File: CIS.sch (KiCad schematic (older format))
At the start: 181 parts, among them J2 RJ45_Abracon_ARJP11A-MASA-B-A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, J3 SJ1-3533NG, J4 DEBUG TAG, K1 K_0073, K2 K_0072, P3 K_0023, Q1 Q_0002, Q2 Q_0002, Q3 Q_0002, SW1 SW_0003, SW2 SW_0003, SW3 SW_0003, SW4 SW_0003, SW5 SW_0003, U1 U_0076, U14 U_0101, U16 U_0049, U17 U_0049, U2 U_0131, U3 U_0103, U4 U_0134, U5 U_0081, U6 U_0097, U7 U_0132, U8 U_0133

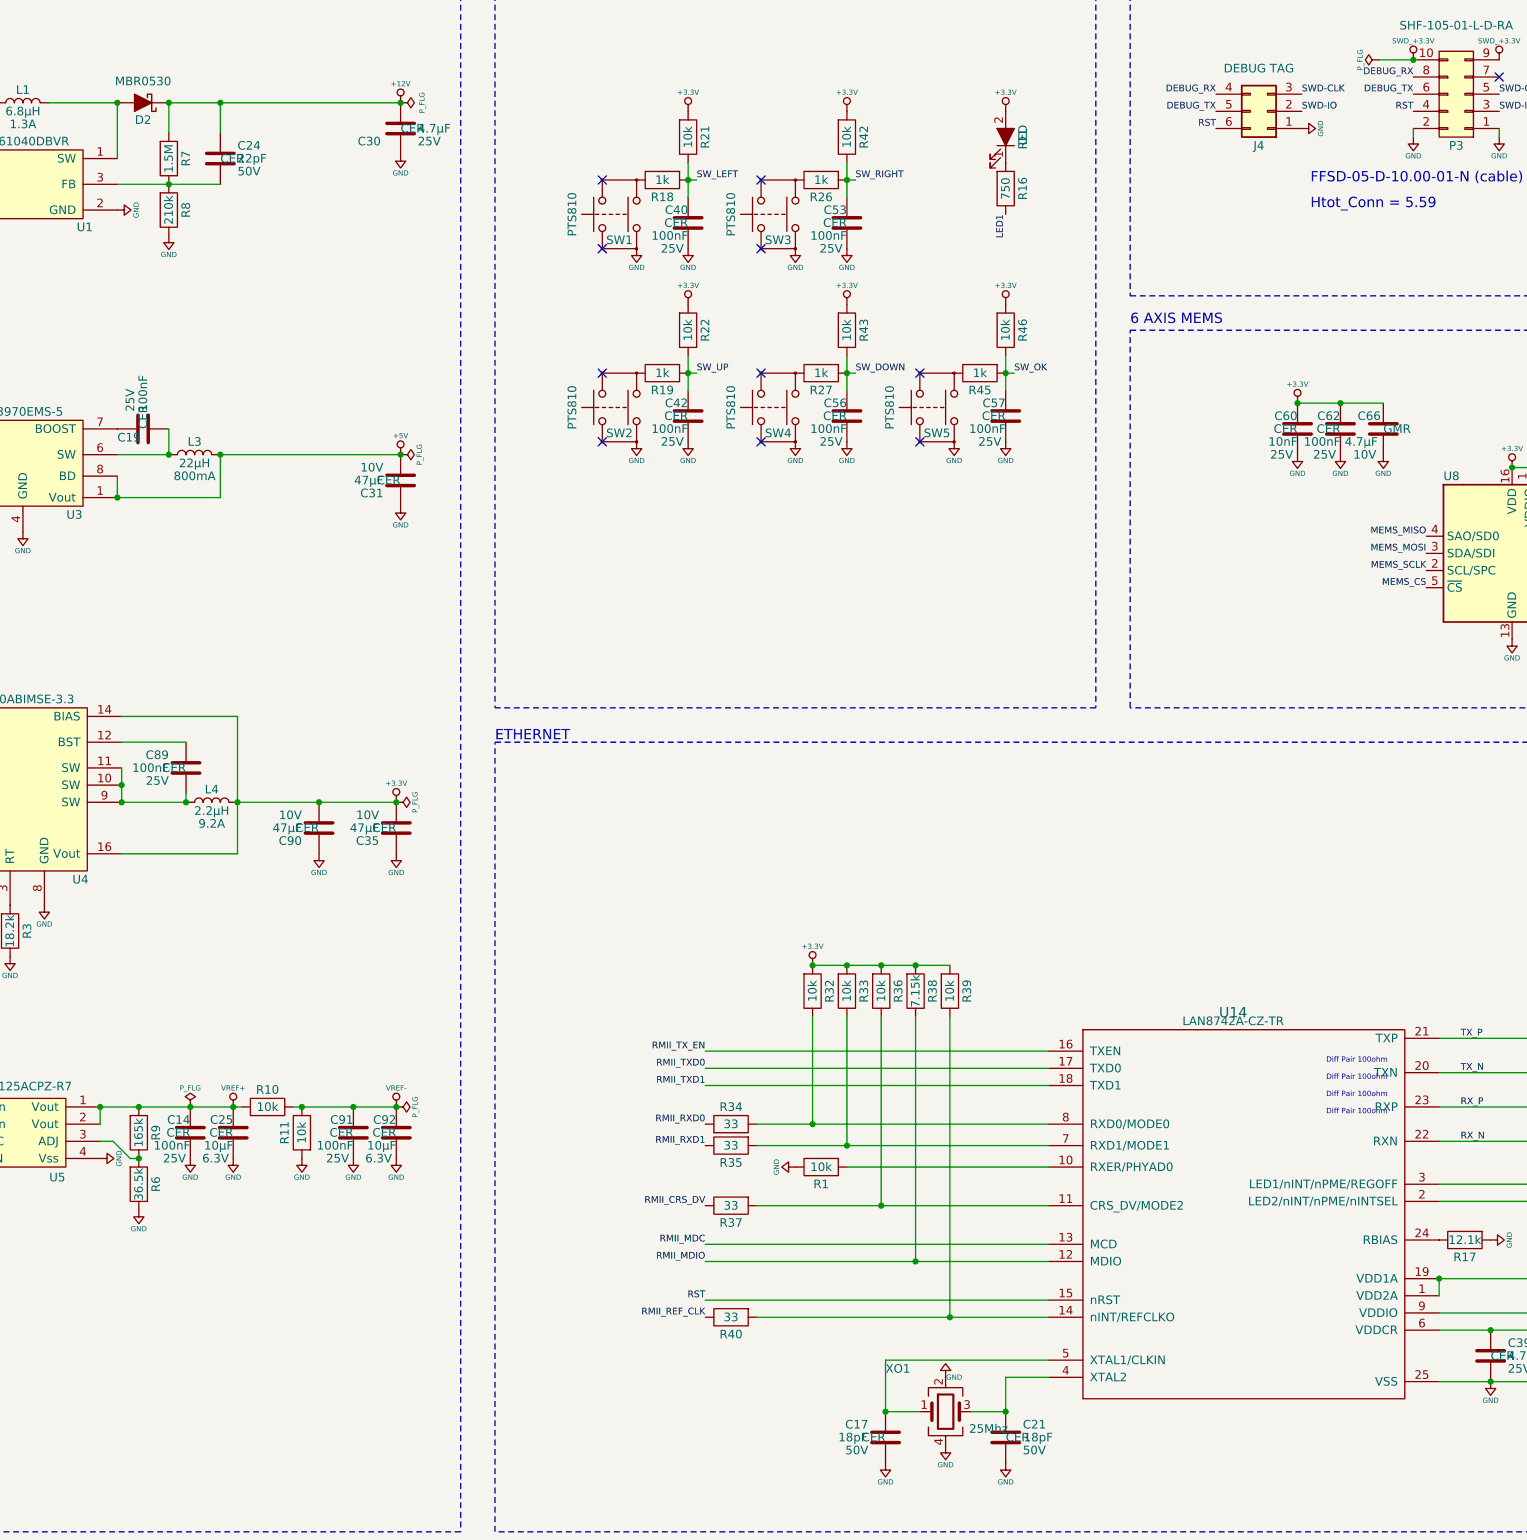
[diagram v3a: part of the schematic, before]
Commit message: Change some DC/DC resistors
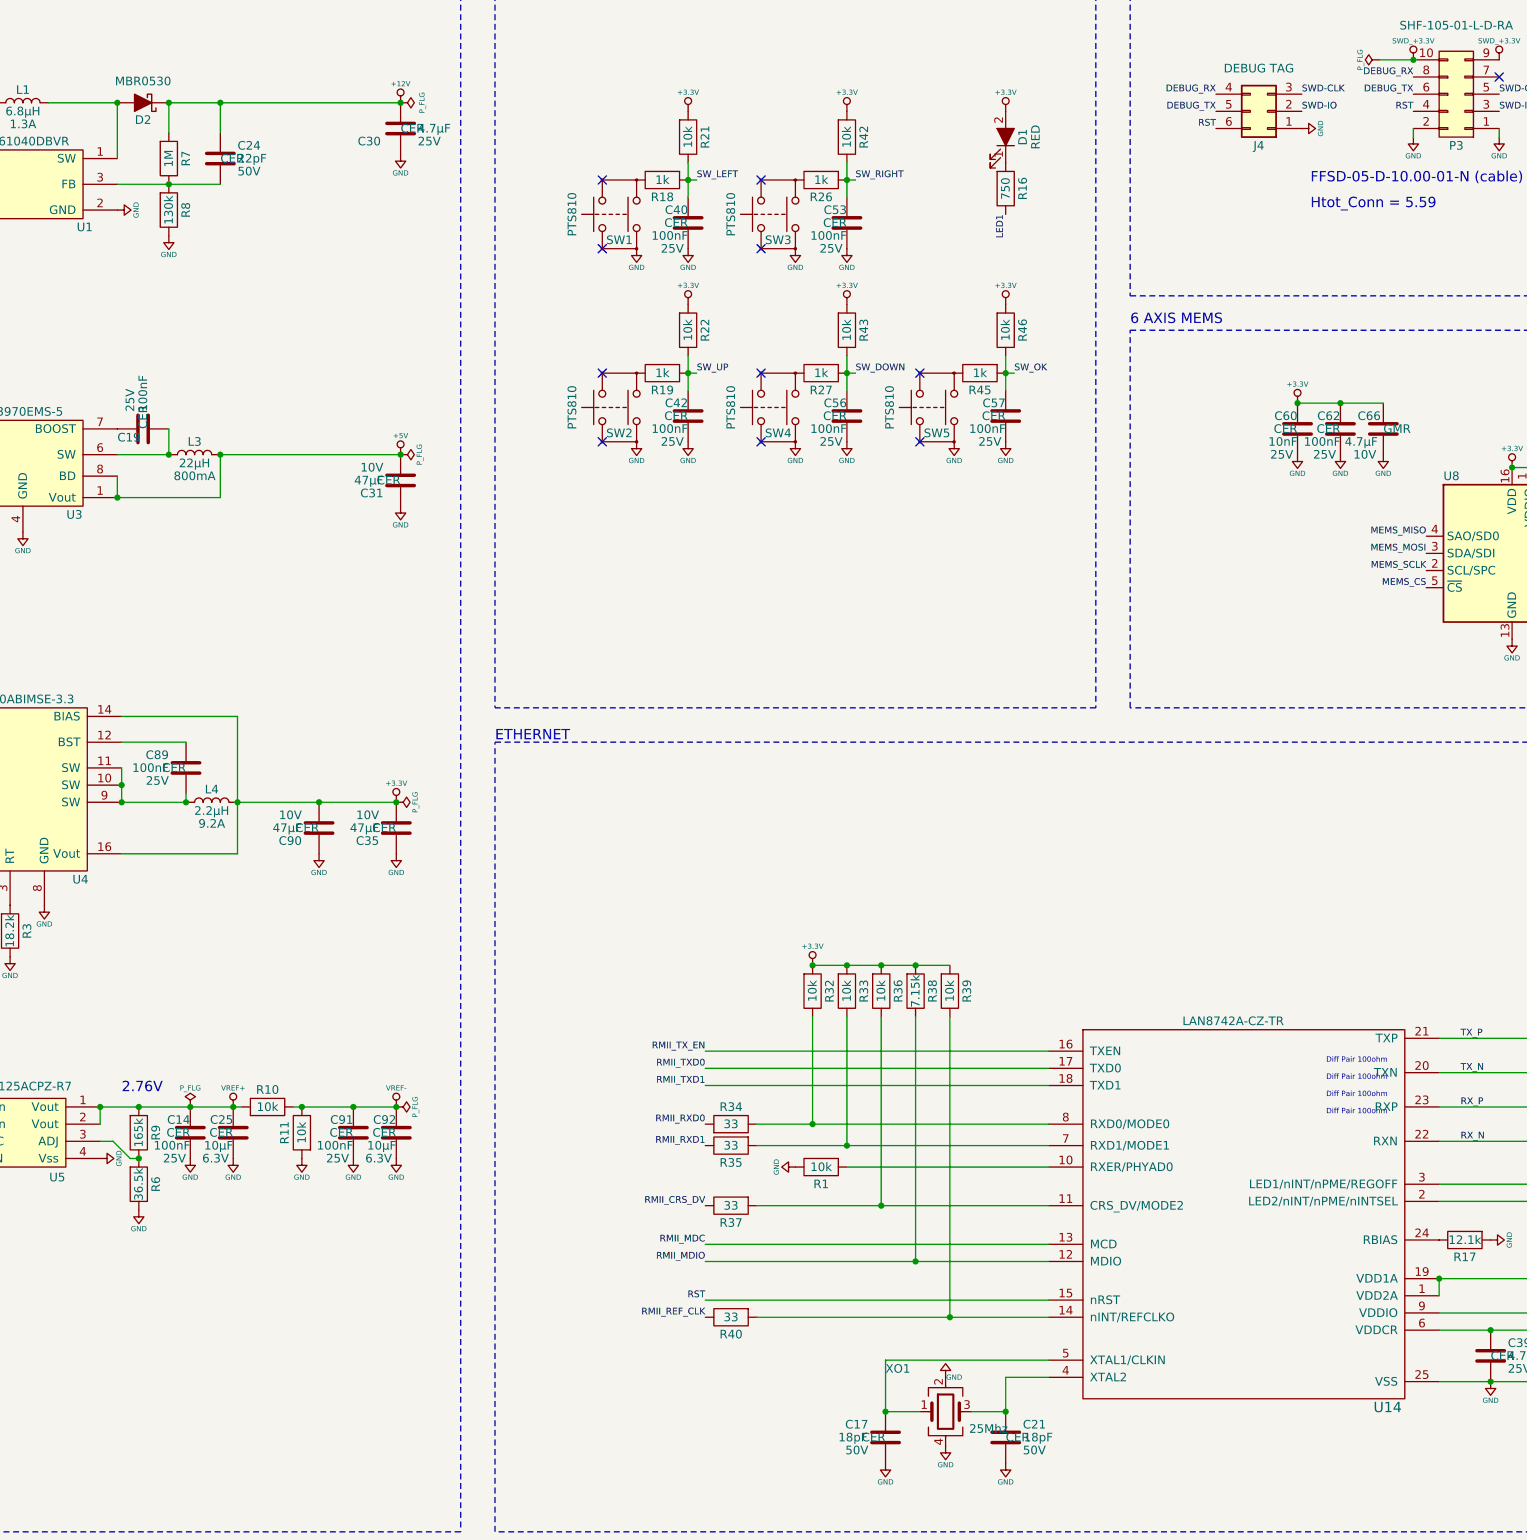
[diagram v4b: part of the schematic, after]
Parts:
- removed R7: R_0107, DVB_Resistors:R_0402, symbol DVB_R:R_0107
- removed R8: R_0108, DVB_Resistors:R_0402, symbol DVB_R:R_0108
- added R7: R_0002, DVB_Resistors:R_0402, symbol DVB_R:R_0002
- added R8: R_0114, DVB_Resistors:R_0402, symbol DVB_R:R_0114
- R10, R11: value NC -> R_0020
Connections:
- net +12V: now also R7.1
- net GND: now also R8.2
- net at C24.2, U1.3 (FB): now also R7.2, R8.1
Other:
- note added: "2.76V"
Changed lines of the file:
@@
 	3625 13325 3575 13325
 Wire Wire Line
-	3925 13325 3975 13325
-Connection ~ 3975 13325
-Wire Wire Line
-	3975 13325 4275 13325
-Wire Wire Line
 	2800 13525 2875 13525
 Wire Wire Line
@@
 F 5 "2mA" H 8075 7025 50  0001 C CNN "Field5"
 F 6 "LED" H 8075 7125 50  0001 C CNN "Field6"
-F 7 "RED" H 8075 7775 50  0000 C CNN "Field7"
+F 7 "RED" H 8075 7850 50  0000 C CNN "Field7"
 F 8 "TOP" H 8075 6925 50  0001 C CNN "Field8"
 	1    8075 7675
@@
 U 1 1 5B700079
 P 9400 13675
-F 0 "U14" H 9400 14575 60  0000 C CNN
+F 0 "U14" H 10300 12275 60  0000 C CNN
 F 1 "U_0101" H 9400 14675 60  0001 C CNN
 F 2 "DVB_QFN:QFN-24-1EP_4x4mm_Pitch0.5mm" H 9400 12075 50  0001 C CNN
@@
 $EndComp
 $Comp
-L DVB_R:R_0108 R8
-U 1 1 5FC77FC4
-P 3200 8100
-F 0 "R8" V 3300 8100 50  0000 C CNN
-F 1 "R_0108" H 3200 7900 50  0001 C CNN
-F 2 "DVB_Resistors:R_0402" H 3200 7750 50  0001 C CNN
-F 3 "generic" H 3200 7825 50  0001 C CNN
-F 4 "210k" V 3200 8100 50  0000 C CNN "Field4"
-F 5 "1%" V 2950 8000 50  0001 L CNN "Field5"
-F 6 "100mW" V 3025 8000 50  0001 L CNN "Field6"
-	1    3200 8100
-	1    0    0    -1
-$EndComp
-$Comp
-L DVB_R:R_0107 R7
-U 1 1 5FC7A17A
-P 3200 7800
-F 0 "R7" V 3300 7800 50  0000 C CNN
-F 1 "R_0107" H 3200 7600 50  0001 C CNN
-F 2 "DVB_Resistors:R_0402" H 3200 7450 50  0001 C CNN
-F 3 "generic" H 3200 7525 50  0001 C CNN
-F 4 "1.5M" V 3200 7800 50  0000 C CNN "Field4"
-F 5 "5%" V 2950 7700 50  0001 L CNN "Field5"
-F 6 "100mW" V 3025 7700 50  0001 L CNN "Field6"
-	1    3200 7800
-	1    0    0    -1
-$EndComp
-$Comp
 L DVB_D:D_0021 D2
 U 1 1 5FC7C0CC
@@
 $EndComp
 $Comp
-L DVB_R:R_0020 R10
-U 1 1 600F96BA
-P 3775 13325
-F 0 "R10" V 3875 13325 50  0000 C CNN
-F 1 "NC" H 3775 13125 50  0001 C CNN
-F 2 "DVB_Resistors:R_0402" H 3775 12975 50  0001 C CNN
-F 3 "generic" H 3775 13050 50  0001 C CNN
-F 4 "10k" V 3775 13325 50  0000 C CNN "Field4"
-F 5 "1%" V 3525 13225 50  0001 L CNN "Field5"
-F 6 "100mW" V 3600 13225 50  0001 L CNN "Field6"
-	1    3775 13325
-	0    -1   -1   0
-$EndComp
-$Comp
 L DVB_Power:VREF- #PWR0134
 U 1 1 6006BE37
@@
 $EndComp
 $Comp
-L DVB_R:R_0020 R11
-U 1 1 60493085
-P 3975 13475
-F 0 "R11" V 4075 13475 50  0000 C CNN
-F 1 "NC" H 3975 13275 50  0001 C CNN
-F 2 "DVB_Resistors:R_0402" H 3975 13125 50  0001 C CNN
-F 3 "generic" H 3975 13200 50  0001 C CNN
-F 4 "10k" V 3975 13475 50  0000 C CNN "Field4"
-F 5 "1%" V 3725 13375 50  0001 L CNN "Field5"
-F 6 "100mW" V 3800 13375 50  0001 L CNN "Field6"
-	1    3975 13475
-	-1   0    0    1
-$EndComp
-$Comp
 L DVB_R:R_0102 R9
 U 1 1 5FF5F2BC
@@
 Connection ~ 2925 11450
 Connection ~ 2925 11550
+Text Notes 2925 13250 0    60   ~ 0
+2.76V
+$Comp
+L DVB_R:R_0020 R10
+U 1 1 606EB751
+P 3775 13325
+F 0 "R10" V 3875 13325 50  0000 C CNN
+F 1 "R_0020" H 3775 13125 50  0001 C CNN
+F 2 "DVB_Resistors:R_0402" H 3775 12975 50  0001 C CNN
+F 3 "generic" H 3775 13050 50  0001 C CNN
+F 4 "10k" V 3775 13325 50  0000 C CNN "Field4"
+F 5 "1%" V 3525 13225 50  0001 L CNN "Field5"
+F 6 "100mW" V 3600 13225 50  0001 L CNN "Field6"
+	1    3775 13325
+	0    -1   -1   0
+$EndComp
+$Comp
+L DVB_R:R_0020 R11
+U 1 1 606EBF59
+P 3975 13475
+F 0 "R11" V 4075 13475 50  0000 C CNN
+F 1 "R_0020" H 3975 13275 50  0001 C CNN
+F 2 "DVB_Resistors:R_0402" H 3975 13125 50  0001 C CNN
+F 3 "generic" H 3975 13200 50  0001 C CNN
+F 4 "10k" V 3975 13475 50  0000 C CNN "Field4"
+F 5 "1%" V 3725 13375 50  0001 L CNN "Field5"
+F 6 "100mW" V 3800 13375 50  0001 L CNN "Field6"
+	1    3975 13475
+	-1   0    0    1
+$EndComp
+Wire Wire Line
+	3925 13325 3975 13325
+Connection ~ 3975 13325
+Wire Wire Line
+	3975 13325 4275 13325
+$Comp
+L DVB_R:R_0002 R7
+U 1 1 607436DA
+P 3200 7800
+F 0 "R7" V 3300 7800 50  0000 C CNN
+F 1 "R_0002" H 3200 7600 50  0001 C CNN
+F 2 "DVB_Resistors:R_0402" H 3200 7450 50  0001 C CNN
+F 3 "generic" H 3200 7525 50  0001 C CNN
+F 4 "1M" V 3200 7800 50  0000 C CNN "Field4"
+F 5 "1%" V 2950 7700 50  0001 L CNN "Field5"
+F 6 "100mW" V 3025 7700 50  0001 L CNN "Field6"
+	1    3200 7800
+	1    0    0    -1
+$EndComp
+$Comp
+L DVB_R:R_0114 R8
+U 1 1 60748699
+P 3200 8100
+F 0 "R8" V 3300 8100 50  0000 C CNN
+F 1 "R_0114" H 3200 7900 50  0001 C CNN
+F 2 "DVB_Resistors:R_0402" H 3200 7750 50  0001 C CNN
+F 3 "generic" H 3200 7825 50  0001 C CNN
+F 4 "130k" V 3200 8100 50  0000 C CNN "Field4"
+F 5 "1%" V 2950 8000 50  0001 L CNN "Field5"
+F 6 "63mW" V 3025 8000 50  0001 L CNN "Field6"
+	1    3200 8100
+	1    0    0    -1
+$EndComp
 $EndSCHEMATC

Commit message: Update shematic
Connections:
- net SW_DOWN renamed SW_1
- net SW_LEFT renamed SW_4
- net SW_OK renamed SW_3
- net SW_RIGHT renamed SW_5
- net SW_UP renamed SW_2
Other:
- note added: "1.8M"
- note added: "126mV"
- note added: "205K"
- note added: "22.1"
- note added: "23.7\n"
- note added: "392"
- note added: "4.7pF"
- note added: "43.2"
- note added: "470pF"
- note added: "49.9ohm"
- note added: "8K2"
- note added: "NC"
- moved on the sheet: C40, C42, C53, C56, C57, D1, R16, R18, R19, R21, R22, R26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
